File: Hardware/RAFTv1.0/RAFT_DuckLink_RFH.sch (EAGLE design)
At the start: 70 parts, among them J1 AMPHENOL_132134, J2 132134-15, J3 AMPHENOL_132134, U1 SX1276, U2 MAX2771ETI+, U3 ESP32-D0WD, U4 W25Q16BVSSIG, U6 PE4259, Y1 32.768kHz

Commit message: added all designs to DuckLink schematic. renamed library
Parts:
- added C47, C48, C63, C64, C65: 10uF, GRM155C80J106ME11D:GRM155C80J106ME11D
- added C49, C55, C56, C62: 0.1uF, GRM155R71C104KA88D:GRM155R71C104KA88D
- added C50: 10pF, GCM1555C1H100JA16J:GCM1555C1H100JA16J
- added C51, C52, C53: 22uF, CL05A226MQ5N6J8:CL05A226MQ5N6J8
- added C54, C59, C60, C61: 1.0uF, GCM155C71A105KE38D:GCM155C71A105KE38D
- added C57, C66: 4.7uF, GRM155R60J475ME87D:GRM155R60J475ME87D
- added C58: 2.2uF, GRM155D80J225ME95D:GRM155D80J225ME95D
- added C67: 22pF, GCM1555C1H220JA16J:GCM1555C1H220JA16J
- added D1: PDS1040-13, PDS1040-13:PDS1040-13
- added D2: BAT54C, diode:BAT54C
- added D3, D4: LTST-C190GKT, LTST-C190GKT:LTST-C190GKT
- added IC1: TPS63060, texas:TPS63060
- added J4: Micro-USB, 105017-0001:105017-0001FIXED
- added L10: 10uH, rcl:L-USL3225M
- added L9: 1uH, DFE2HCAH1R0MJ0L:DFE2HCAH1R0MJ0L
- added Q1_Q2: SI7288DP-T1-GE3, SI7288DP-T1-GE3:SI7288DP-T1-GE3
- added Q3: 2N7002, 2N7002:2N7002
- added R10, R6: 100k, CRCW0402100KFKED:CRCW0402100KFKED
- added R11, R12: 499k, CRCW0402499KFKED:CRCW0402499KFKED
- added R13: 36k, CRCW040236K0FKED:CRCW040236K0FKED
- added R14: 2k, CRCW04022K00FKED:CRCW04022K00FKED
- added R15: 10, CRCW040210R0JNEDC:CRCW040210R0JNEDC
- added R16, R17: 10K, CRCW040210K0JNED:CRCW040210K0JNED
- added R18: 499R, rcl-raft:CRCW0402499RFKEDC
- added R5: 1M, ERJ-2RKF1004X:ERJ-2RKF1004X
- added R7: 560k, ERJ-2GEJ564X:ERJ-2GEJ564X
- added R8: 4.7k, CRCW04024K70JNEDC:CRCW04024K70JNEDC
- added R9: 10k, CRCW040210K0JNED:CRCW040210K0JNED
- added R_SR: 20m, ERJ-3BWFR020V:ERJ-3BWFR020V
- added U5: INTERFACE-CP2102-GMR(QFN28), INTERFACE-CP2102-GMR_QFN28_:INTERFACE-CP2102-GMR(QFN28)
- added U7: SP0503BAHT, SP0503BAHT:SP0503BAHT
- added U8: BQ24650RVAR, TexasInstruments:BQ24650RVAR
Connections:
- new net /CE: Q3.G
- new net 3V3_EN: IC1.EN
- new net N$29: IC1.L2, L9.2
- new net N$44: IC1.L1, L9.1
- new net N$46: C49.2, IC1.VAUX
- new net N$48: IC1.PG, R5.1
- new net N$49: C50.2, IC1.FB, R6.2, R7.1
- new net N$50: R8.1, U5.!RST
- new net N$51: R9.1, U5.!SUSPEND
- new net N$52: C54.2, C55.2, J4.VDD, U5.REGIN, U5.VBUS, U7.A
- new net N$53: C56.2, C57.2, U5.VDD
- new net N$54: J4.D-, U5.D-, U7.C
- new net N$55: J4.D+, U5.D+, U7.B
- new net N$56: J4.GND, U7.GND
- new net N$57: C60.1, U8.TERM_EN, U8.VREF
- new net N$58: Q3.D, R12.1, R13.2, U8.MPPSET
- new net N$59: C59.1, R15.2, U8.VCC
- new net N$60: C61.1, D2.A1, D2.A2, U8.REGN
- new net N$61: C62.2, D2.CC, U8.BTST
- new net N$62: C67.1, R10.2, R11.1, U8.VFB
- new net N$63: C64.1, L10.2, R_SR.1, U8.SRP
- new net N$64: Q3.S
- new net N$65: D4.A2, R17.2
- new net N$66: D3.A2, R16.2
- new net N$67: D4.K2, U8.STAT2
- new net N$68: D3.K2, U8.STAT1
- new net N$69: C62.1, L10.1, U8.PH
- new net N$70: Q1_Q2.D2_1, Q1_Q2.S1
- new net N$71: Q1_Q2.G2, U8.LODRV
- new net N$72: C58.2, R14.1
- new net Q1_G: Q1_Q2.G1, U8.HIDRV
- new net SC_VIN: C63.2, D1.K, Q1_Q2.D1_1, R15.1
- new net U0TXD: R18.1, U5.TXD
- new net U0_DTR: U5.DTR
- new net U0_RTS: U5.RTS
- new net VDD: R8.2
- new net VIN: D1.A, R12.2, R14.2, R16.1, R17.1
- new net VIN_BATT: C47.2, C48.2, IC1.VIN
- new net VOUT_BATT: C64.2, C65.2, C66.2, C67.2, R11.2, R_SR.2, U8.SRN
- net +3.3V: now also C51.2, C52.2, C53.2, IC1.VOUT, R5.2, R7.2
- net GND: now also C47.1, C48.1, C49.1, C50.1, C51.1, C52.1, C53.1, C54.1, C55.1, C56.1, C57.1, C58.1, C59.2, C60.2, C61.2, C63.1, C65.1, C66.1, IC1.GND, IC1.PGND, IC1.PS/SYNC, Q1_Q2.S2, R10.1, R13.1, R6.1, R9.2, U5.GND@1, U8.EP, U8.GND
- net N$32: now also R18.2
- net U0RXD: now also U5.RXD
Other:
- note added: "BQ24650RVAR"
- note added: "CP2102"
- note added: "TPS63060DSCR"

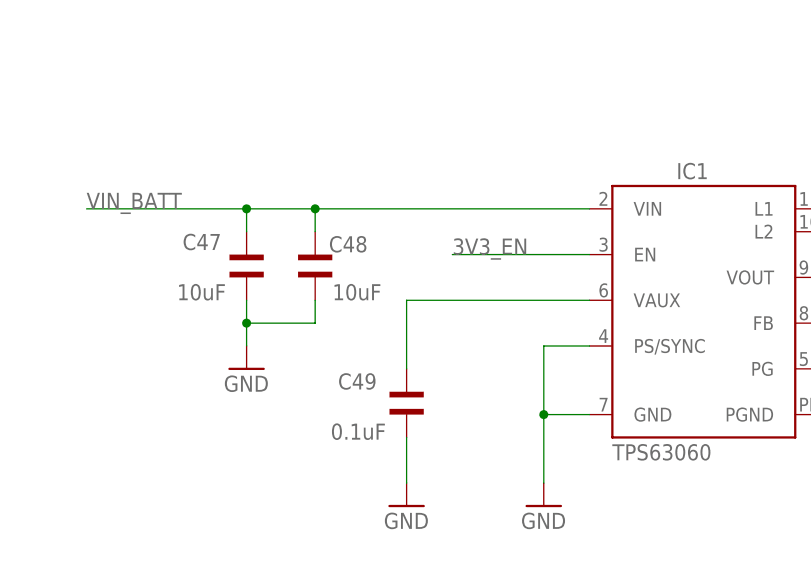
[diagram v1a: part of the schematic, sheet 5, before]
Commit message: added load sharing system
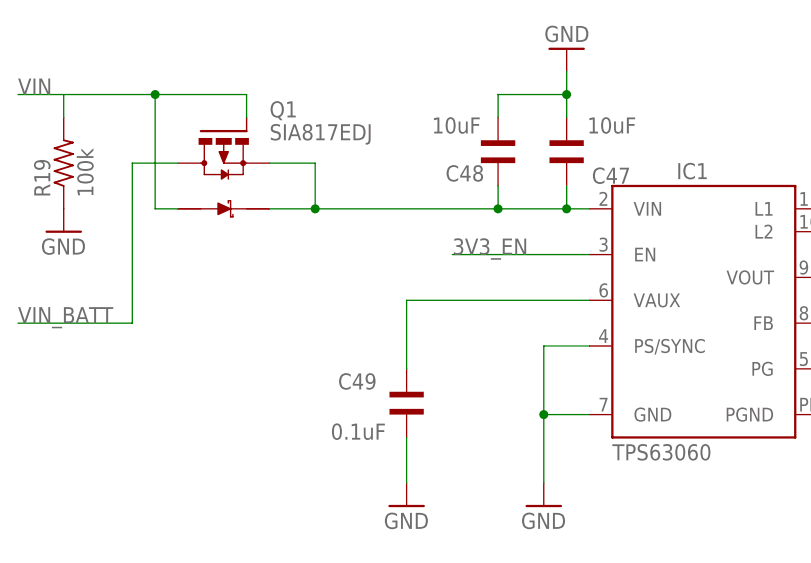
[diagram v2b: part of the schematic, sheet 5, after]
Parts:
- added Q1: SIA817EDJ, RAFT-components:SIA817EDJ
- added R19: 100k, RAFT-components:CRCW0402100KFKED
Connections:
- new net SC_VIN1: R19.2
- new net VIN_SYS: C47.2, C48.2, IC1.VIN, Q1.K, Q1.S
- net GND: now also R19.1
- net VIN: now also Q1.A, Q1.G
- net VIN_BATT: now also Q1.D; no longer C47.2, C48.2, IC1.VIN
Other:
- moved on the sheet: C47, C48, C63, D1

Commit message: consolidated components
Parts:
- removed IC1: TPS63060, texas:TPS63060
- removed Q1_Q2: SI7288DP-T1-GE3, SI7288DP-T1-GE3:SI7288DP-T1-GE3
- added C68: 10uF, GRM155C80J106ME11D:GRM155C80J106ME11D
- added Q2: SI7288DP, RAFT-components:SI7288DP
- added U9: TPS63070RNMT, TPS63070RNMT:TPS63070RNMT
- C47, C48: value 10uF -> 22uF; device GRM155C80J106ME11D:GRM155C80J106ME11D -> RAFT-components:GRM188R60J226MEA0D
- C49: value 0.1uF -> 22uF; device GRM155R71C104KA88D:GRM155R71C104KA88D -> RAFT-components:GRM188R60J226MEA0D
- C50: value 10pF -> 10uF; device GCM1555C1H100JA16J:GCM1555C1H100JA16J -> GRM155C80J106ME11D:GRM155C80J106ME11D
- C51, C53: value 22uF -> 10uF; device CL05A226MQ5N6J8:CL05A226MQ5N6J8 -> GRM155C80J106ME11D:GRM155C80J106ME11D
- C52: value 22uF -> 0.1uF; device CL05A226MQ5N6J8:CL05A226MQ5N6J8 -> GRM155R71C104KA88D:GRM155R71C104KA88D
- L10: device rcl:L-USL3225M -> RAFT-components:LQM18FN100M00D
- L9: value 1uH -> 1.5uH; device DFE2HCAH1R0MJ0L:DFE2HCAH1R0MJ0L -> RAFT-components:LQM18PN1R5MFRL
- R11, R12: value 499k -> 499R; device CRCW0402499KFKED:CRCW0402499KFKED -> RAFT-components:CRCW0402499RFKEDC
- R5: value 1M -> 100k; device ERJ-2RKF1004X:ERJ-2RKF1004X -> CRCW0402100KFKED:CRCW0402100KFKED
- R6: value 100k -> 470k; device CRCW0402100KFKED:CRCW0402100KFKED -> RAFT-components:CRCW0402470KFKEDC
- R7: value 560k -> 150k; device ERJ-2GEJ564X:ERJ-2GEJ564X -> RAFT-components:CRCW0402150KFKEDC
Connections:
- removed net 3V3_EN: IC1.EN
- removed net N$70: Q1_Q2.D2_1, Q1_Q2.S1
- removed net N$71: Q1_Q2.G2, U8.LODRV
- removed net Q1_G: Q1_Q2.G1, U8.HIDRV
- new net +3V3: C47.2, C48.2, C49.2, C53.1, R5.2, R6.1, U9.VOUT
- new net N$45: L9.1, U9.L1
- new net N$47: R5.1, U9.PG
- net +3.3V: no longer C51.2, C52.2, C53.2, IC1.VOUT, R5.2, R7.2
- net GND: now also C53.2, C68.1, Q2.S1, R7.1, U9.FB2, U9.GND, U9.PGND, U9.VSEL; no longer C53.1, IC1.GND, IC1.PGND, IC1.PS/SYNC, Q1_Q2.S2, R6.1
- net N$29: now also C52.2, U9.VAUX; no longer IC1.L2, L9.2
- net N$44: now also Q2.G, U8.HIDRV; no longer IC1.L1, L9.1
- net N$46: now also L9.2, U9.L2; no longer C49.2, IC1.VAUX
- net N$48: now also Q2.G1, U8.LODRV; no longer IC1.PG, R5.1
- net N$49: now also R7.2, U9.FB; no longer C50.2, IC1.FB, R7.1
- net N$63: now also Q2.D1, Q2.S
- net SC_VIN: now also Q2.D; no longer Q1_Q2.D1_1
- net VIN_SYS: now also C50.2, C51.2, C68.2, U9.VIN; no longer C47.2, C48.2, IC1.VIN
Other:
- note added: "1.1"
- note added: "TPS63070DSCR"
- note removed: "TPS63060DSCR"
- moved on the sheet: C50, C51, C52, C53, C63, L10, Q1, R19, R5, R6, R7

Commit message: CAP connection and 2G4 antenna switch for MCU
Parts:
- removed J3: AMPHENOL_132134, AmphenolRF:AMPHENOL_132134
- added C69: 1nF, rcl-raft:GCM155R71H102KA37D
- added C70: 3.3nF, RAFT-components:GCM155R71H332KA37D
- added C71: 10uF, RAFT-components:GRM155C80J106ME11D
- added J5: 132134-15, 132134-15:132134-15
- added R20: 20k, RAFT-components:CRCW040220K0FKEDC
- added U10: PE4259, PE4259:PE4259
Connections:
- net ANT_SEL renamed GPS_ANT_SEL
- net OC_ANT renamed GPS_INT_ANT
- removed net GPIO35: U3.VDET_2
- removed net VIN_BATT: Q1.D
- new net 2G4_ANT_SEL: U10.CTRL, U3.VDET_2
- new net 2G4_INT_ANT: U10.RF1
- new net N$70: J5.SIG, U10.RF2
- new net N$71: C70.1, R20.2, U3.CAP2
- new net N$74: C70.2, C71.1, R20.1, U3.CAP1
- net +3.3V: now also C69.2, U10.!CTRL/!VDD
- net GND: now also C69.1, C71.2, U10.GND
- net N$41: now also U10.RFC; no longer J3.SIG
- net VOUT_BATT: now also Q1.D

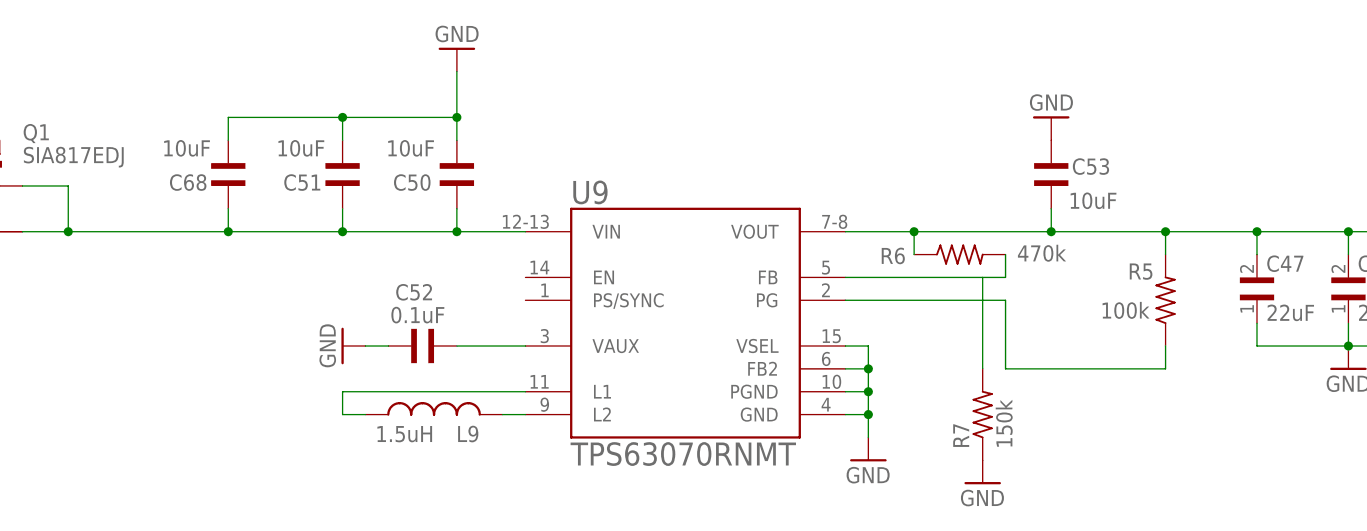
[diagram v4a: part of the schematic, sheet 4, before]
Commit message: fixed component inconsistencies
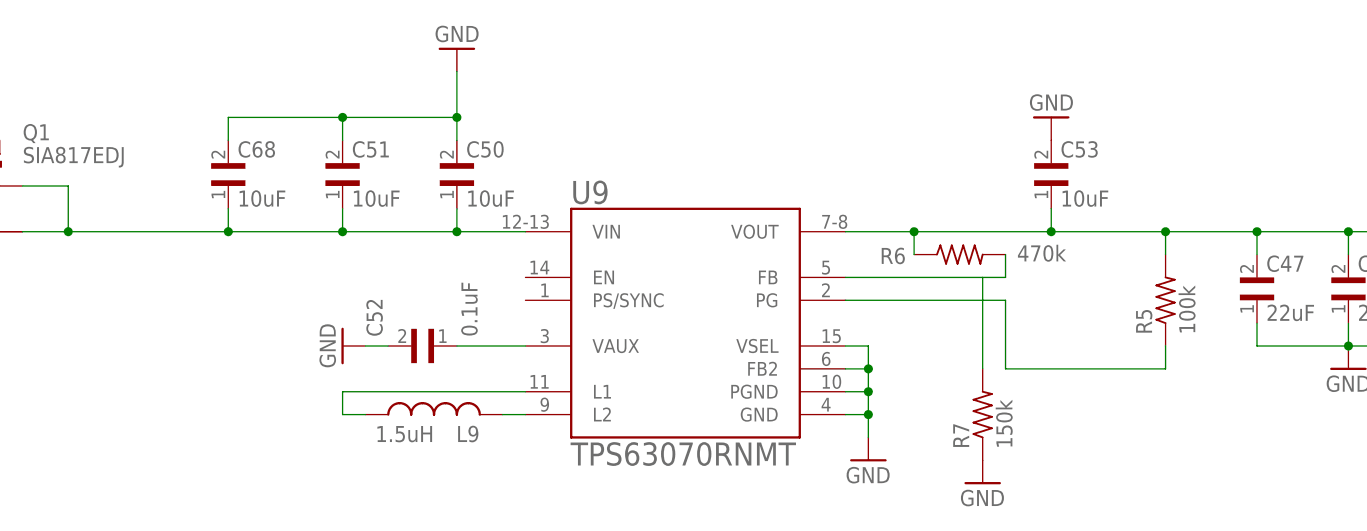
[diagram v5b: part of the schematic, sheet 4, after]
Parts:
- C40: device rcl-raft:GRM155C80J106ME11D -> RAFT-components:GRM155C80J106ME11D
- C50, C51, C53, C63, C64, C65, C68: device GRM155C80J106ME11D:GRM155C80J106ME11D -> RAFT-components:GRM155C80J106ME11D
- C52, C55, C56, C62: device GRM155R71C104KA88D:GRM155R71C104KA88D -> RAFT-components:GCM155R71C104KA55J
- J2: value 132134-15 -> AMPHENOL_132134; device 132134-15:132134-15 -> AmphenolRF:AMPHENOL_132134
- R10, R5: device CRCW0402100KFKED:CRCW0402100KFKED -> RAFT-components:CRCW0402100KFKED
- R9: device CRCW040210K0JNED:CRCW040210K0JNED -> RAFT-components:CRCW040210K0JNED
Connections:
- removed net N$44: Q2.G, U8.HIDRV
- net GND: now also C50.2, C51.2, C52.2, C68.2; no longer C50.1, C51.1, C52.1, C68.1
- net N$29: now also C52.1; no longer C52.2
- net N$61: now also Q2.G, U8.HIDRV
- net N$63: now also C64.2; no longer C64.1
- net VIN_SYS: now also C50.1, C51.1, C68.1; no longer C50.2, C51.2, C68.2
- net VOUT_BATT: now also C64.1; no longer C64.2

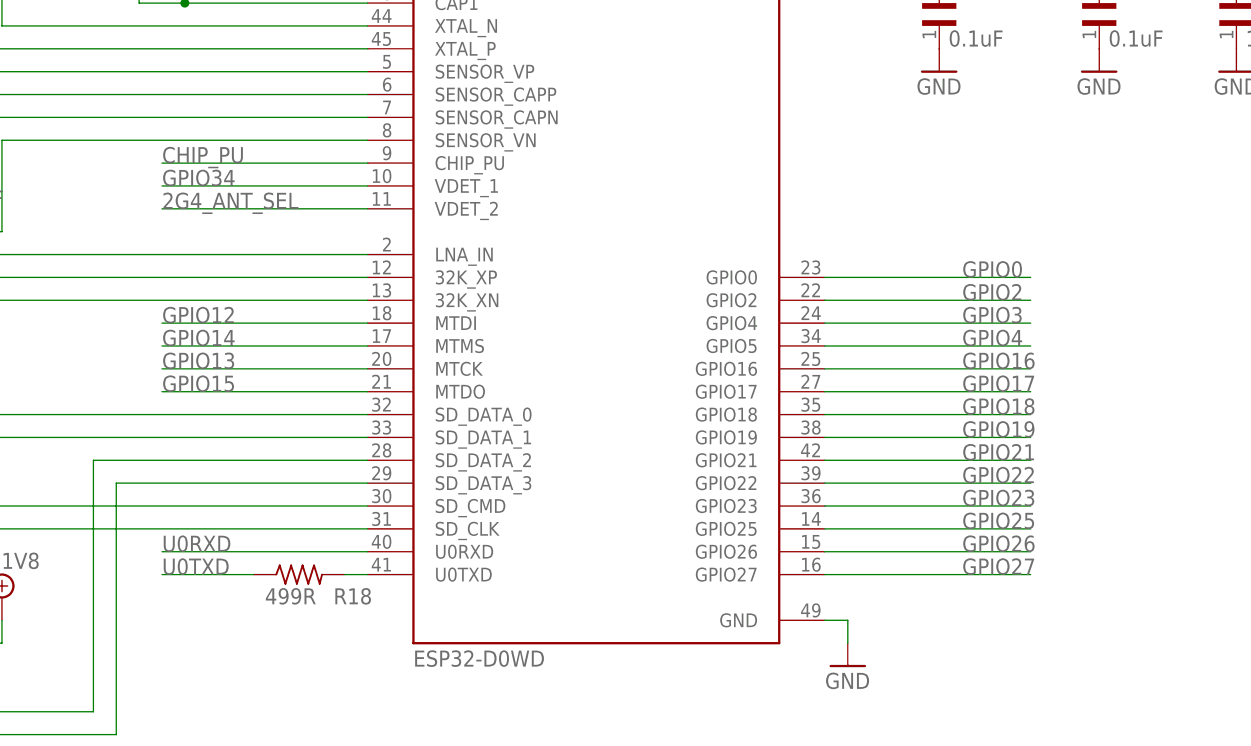
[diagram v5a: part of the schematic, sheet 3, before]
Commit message: final gpio connections
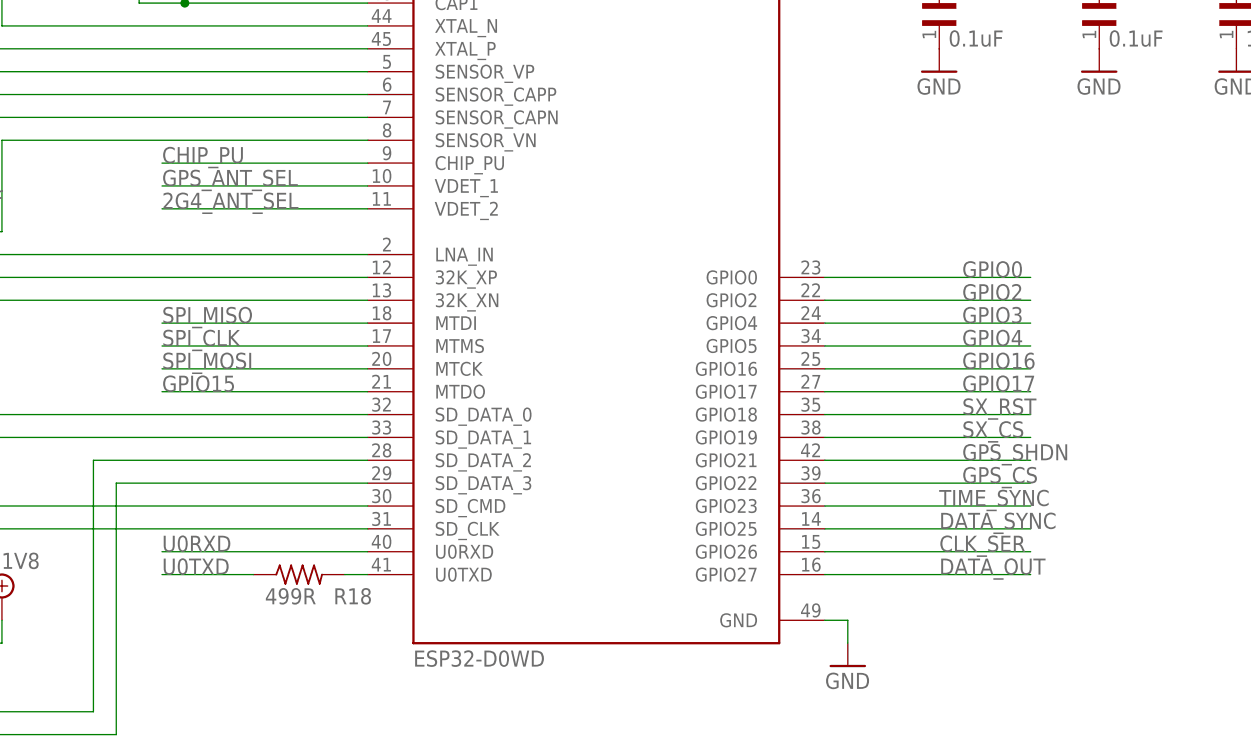
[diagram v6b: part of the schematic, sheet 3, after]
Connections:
- removed net GPIO12: U3.MTDI
- removed net GPIO13: U3.MTCK
- removed net GPIO14: U3.MTMS
- removed net GPIO18: U3.GPIO18
- removed net GPIO19: U3.GPIO19
- removed net GPIO21: U3.GPIO21
- removed net GPIO22: U3.GPIO22
- removed net GPIO23: U3.GPIO23
- removed net GPIO25: U3.GPIO25
- removed net GPIO26: U3.GPIO26
- removed net GPIO27: U3.GPIO27
- removed net GPIO34: U3.VDET_1
- removed net GPS_SCLK: U2.SCLK
- removed net GPS_SDATA: U2.SDATA
- removed net MISO: U1.MISO
- removed net MOSI: U1.MOSI
- new net SPI_MISO: U1.MISO, U3.MTDI
- new net SPI_MOSI: U1.MOSI, U2.SDATA, U3.MTCK
- net CLK_SER: now also U3.GPIO26
- net DATA_OUT: now also U3.GPIO27
- net DATA_SYNC: now also U3.GPIO25
- net GPS_ANT_SEL: now also U3.VDET_1
- net GPS_CS: now also U3.GPIO22
- net GPS_SHDN: now also U3.GPIO21
- net SPI_CLK: now also U2.SCLK, U3.MTMS
- net SX_CS: now also U3.GPIO19
- net SX_RST: now also U3.GPIO18
- net TIME_SYNC: now also U3.GPIO23
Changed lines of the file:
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@@
 </segment>
 </net>
-<net name="GPS_SDATA" class="0">
+<net name="SPI_MOSI" class="0">
 <segment>
 <pinref part="U2" gate="G$1" pin="SDATA"/>
@@
 </segment>
 </net>
-<net name="GPS_SCLK" class="0">
+<net name="SPI_CLK" class="0">
 <segment>
 <pinref part="U2" gate="G$1" pin="SCLK"/>
@@
 </segment>
 </net>
-<net name="MOSI" class="0">
+<net name="SPI_MOSI" class="0">
 <segment>
 <wire x1="-25.4" y1="-17.78" x2="-38.1" y2="-17.78" width="0.1524" layer="91"/>
@@
 </segment>
 </net>
-<net name="MISO" class="0">
+<net name="SPI_MISO" class="0">
 <segment>
 <wire x1="-25.4" y1="-20.32" x2="-38.1" y2="-20.32" width="0.1524" layer="91"/>
@@
 </segment>
 </net>
-<net name="GPIO18" class="0">
-<segment>
-<wire x1="48.26" y1="-15.24" x2="25.4" y2="-15.24" width="0.1524" layer="91"/>
-<label x="40.64" y="-15.24" size="1.778" layer="95"/>
-<pinref part="U3" gate="G$1" pin="GPIO18"/>
-</segment>
-</net>
-<net name="GPIO19" class="0">
+<net name="SX_CS" class="0">
 <segment>
 <wire x1="48.26" y1="-17.78" x2="25.4" y2="-17.78" width="0.1524" layer="91"/>
@@
 </segment>
 </net>
-<net name="GPIO21" class="0">
-<segment>
-<wire x1="48.26" y1="-20.32" x2="25.4" y2="-20.32" width="0.1524" layer="91"/>
-<label x="40.64" y="-20.32" size="1.778" layer="95"/>
-<pinref part="U3" gate="G$1" pin="GPIO21"/>
-</segment>
-</net>
-<net name="GPIO22" class="0">
+<net name="GPS_CS" class="0">
 <segment>
 <wire x1="48.26" y1="-22.86" x2="25.4" y2="-22.86" width="0.1524" layer="91"/>
@@
 </segment>
 </net>
-<net name="GPIO23" class="0">
+<net name="TIME_SYNC" class="0">
 <segment>
 <wire x1="48.26" y1="-25.4" x2="25.4" y2="-25.4" width="0.1524" layer="91"/>
-<label x="40.64" y="-25.4" size="1.778" layer="95"/>
+<label x="38.1" y="-25.4" size="1.778" layer="95"/>
 <pinref part="U3" gate="G$1" pin="GPIO23"/>
 </segment>
 </net>
-<net name="GPIO25" class="0">
+<net name="DATA_SYNC" class="0">
 <segment>
 <wire x1="48.26" y1="-27.94" x2="25.4" y2="-27.94" width="0.1524" layer="91"/>
-<label x="40.64" y="-27.94" size="1.778" layer="95"/>
+<label x="38.1" y="-27.94" size="1.778" layer="95"/>
 <pinref part="U3" gate="G$1" pin="GPIO25"/>
 </segment>
 </net>
-<net name="GPIO26" class="0">
+<net name="CLK_SER" class="0">
 <segment>
 <wire x1="48.26" y1="-30.48" x2="25.4" y2="-30.48" width="0.1524" layer="91"/>
-<label x="40.64" y="-30.48" size="1.778" layer="95"/>
+<label x="38.1" y="-30.48" size="1.778" layer="95"/>
 <pinref part="U3" gate="G$1" pin="GPIO26"/>
 </segment>
 </net>
-<net name="GPIO27" class="0">
+<net name="DATA_OUT" class="0">
 <segment>
 <wire x1="48.26" y1="-33.02" x2="25.4" y2="-33.02" width="0.1524" layer="91"/>
-<label x="40.64" y="-33.02" size="1.778" layer="95"/>
+<label x="38.1" y="-33.02" size="1.778" layer="95"/>
 <pinref part="U3" gate="G$1" pin="GPIO27"/>
 </segment>
@@
 </segment>
 </net>
-<net name="GPIO34" class="0">
+<net name="GPS_ANT_SEL" class="0">
 <segment>
 <wire x1="-25.4" y1="10.16" x2="-48.26" y2="10.16" width="0.1524" layer="91"/>
@@
 </segment>
 </net>
-<net name="GPIO13" class="0">
+<net name="SPI_MOSI" class="0">
 <segment>
 <pinref part="U3" gate="G$1" pin="MTCK"/>
@@
 </segment>
 </net>
-<net name="GPIO14" class="0">
+<net name="SPI_CLK" class="0">
 <segment>
 <pinref part="U3" gate="G$1" pin="MTMS"/>
@@
 </segment>
 </net>
-<net name="GPIO12" class="0">
+<net name="SPI_MISO" class="0">
 <segment>
 <pinref part="U3" gate="G$1" pin="MTDI"/>
@@
 </segment>
 </net>
+<net name="GPS_SHDN" class="0">
+<segment>
+<wire x1="48.26" y1="-20.32" x2="25.4" y2="-20.32" width="0.1524" layer="91"/>
+<label x="40.64" y="-20.32" size="1.778" layer="95"/>
+<pinref part="U3" gate="G$1" pin="GPIO21"/>
+</segment>
+</net>
+<net name="SX_RST" class="0">
+<segment>
+<wire x1="48.26" y1="-15.24" x2="25.4" y2="-15.24" width="0.1524" layer="91"/>
+<label x="40.64" y="-15.24" size="1.778" layer="95"/>
+<pinref part="U3" gate="G$1" pin="GPIO18"/>
+</segment>
+</net>
